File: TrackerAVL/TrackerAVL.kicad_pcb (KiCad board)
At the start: 2 copper layers, 120 x 80 mm, 174 parts, among them J801 Conn_02x07_Odd_Even, J802 Conn_01x15, J803 Conn_01x04, P201 uC_debug, Q201 DTC043ZEBTL, Q202 DTC043ZEBTL, Q203 DTC043ZEBTL, Q701 2N7002P, Q702 2N7002P, Q703 2N7002P, Q704 DTC043ZEBTL, U201 MAX3221, U202 LPC4337JBD144, U203 STS8C5H30L, U301 MPU-6050, U401 NAU8814, U501 STS8C5H30L, U502 LD1085D2T33R, U503 NCP114ASN180T1G, U601 MPCIE-Socket, U701 74LVC244APW, U801 74HC4053, X201 12MHz, X202 32.768K

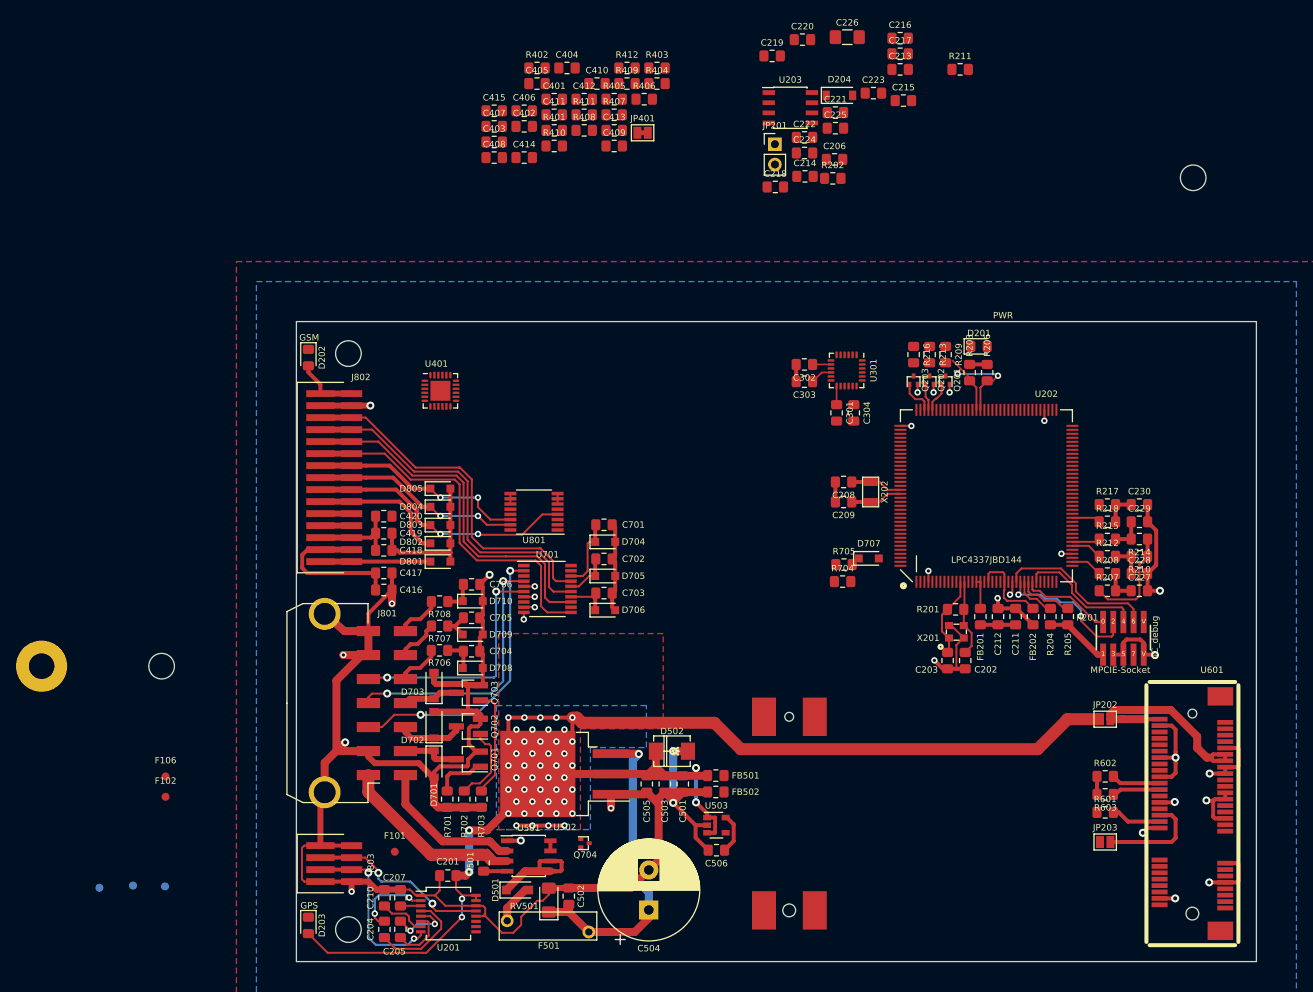
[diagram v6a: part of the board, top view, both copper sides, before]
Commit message: Cambios en pcb y modelos 3d
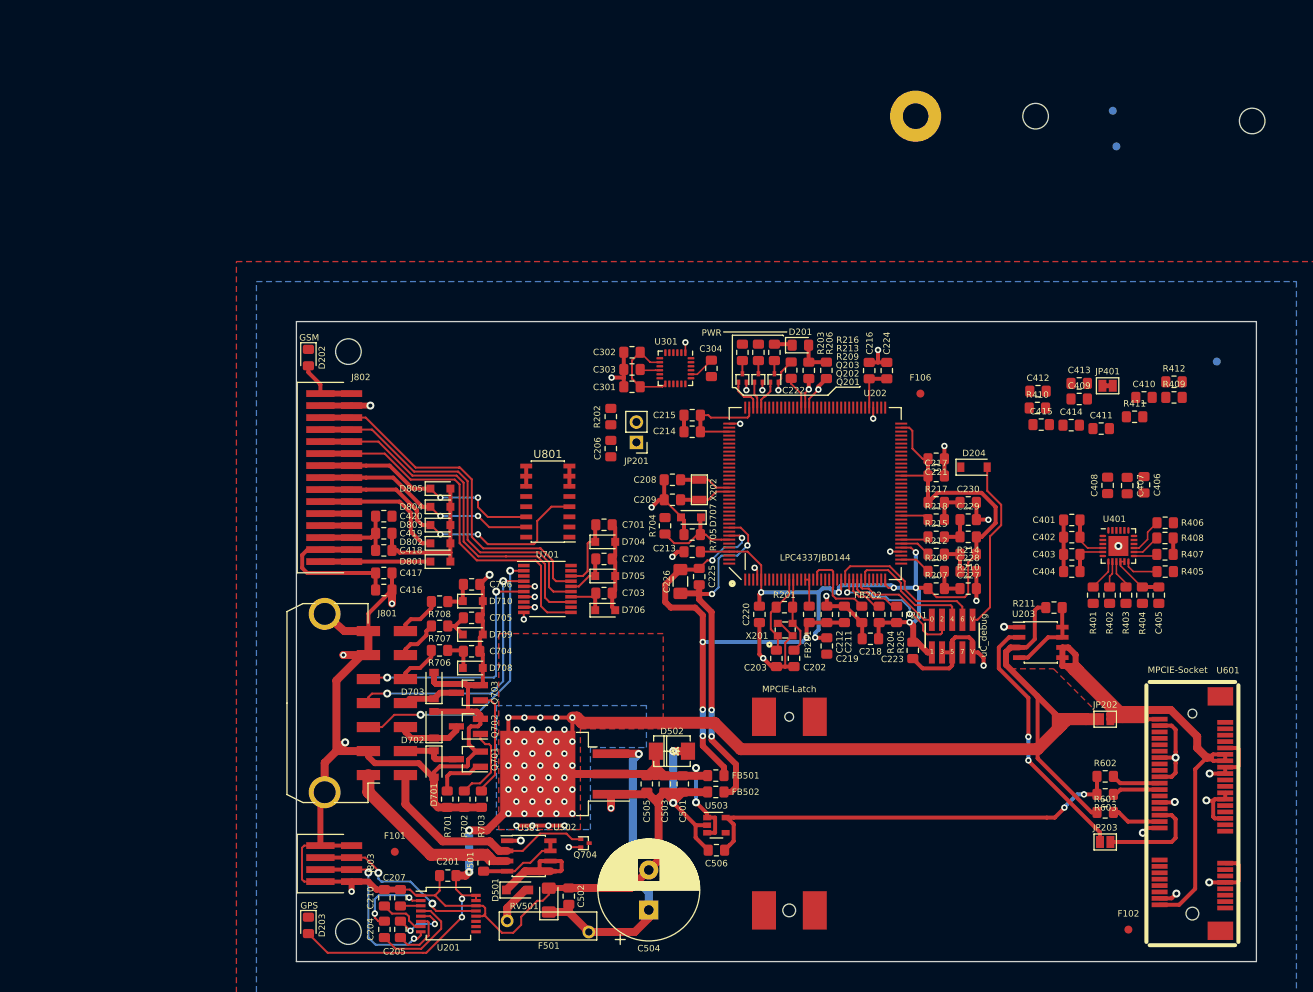
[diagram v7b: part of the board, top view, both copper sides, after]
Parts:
- U801: footprint Package_SO:TSSOP-16_4.4x5mm_P0.65mm -> Package_SO:SOIC-16_3.9x9.9mm_P1.27mm
- moved F103 157.3 mm to (212.5, 48.1)
- moved F104 156.1 mm to (212.1, 43.6)
- moved F105 146.9 mm to (225.1, 75.0)
- moved H102 129.1 mm to (202.4, 44.3)
- moved TP101 129.1 mm to (187.4, 44.3)
- moved F102 121.5 mm to (214.0, 146.0)
- moved F106 105.8 mm to (188.0, 79.0)
- moved C405 100.7 mm to (217.8, 104.2), turned to 270 degrees
- moved R402 97.3 mm to (211.7, 104.2), turned to 270 degrees
- moved C407 91.0 mm to (213.8, 90.5), turned to 270 degrees
- moved R405 90.7 mm to (218.6, 101.2)
- moved C406 90.5 mm to (215.9, 90.4), turned to 270 degrees
- moved C404 89.1 mm to (206.9, 101.2), turned to 180 degrees
- moved R401 89.0 mm to (209.6, 104.2), turned to 270 degrees
- moved C403 88.7 mm to (206.9, 99.1), turned to 180 degrees
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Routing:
- net +3V3: track 215.5 -> 387.0 mm, vias 52 -> 58
- net /CPU/PWR_MDM: track 27.7 -> 87.0 mm
- net +3.3VADC: track 4.40 -> 62.5 mm, vias 0 -> 6
- net +1V8: track 7.30 -> 62.8 mm, vias 0 -> 2
- net GND: track 366.3 -> 414.2 mm, vias 29 -> 38
- net GNDA: track 0.00 -> 46.1 mm, vias 0 -> 4
- net /CPU/GPIO7: track 0.00 -> 32.6 mm, vias 0 -> 2
- net /CPU/RESET_DBG: track 0.00 -> 21.6 mm
- net /CPU/VBAT: track 0.00 -> 11.4 mm
- net /IGN: track 18.8 -> 29.2 mm
- net Net-(R211-Pad1): track 0.00 -> 10.2 mm
- net Net-(C405-Pad1): track 0.00 -> 6.91 mm
- net Net-(R501-Pad1): track 4.22 -> 10.7 mm
- net /I2C_SCL: track 10.7 -> 4.52 mm, vias 2 -> 1
- net Net-(R406-Pad1): track 0.00 -> 4.71 mm
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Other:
- net class Default: via_dia 1 -> 0.8; via_drill 0.5 -> 0.4
- board text added: "MPCIE-Latch"
- board text added: "Net +3V3 Exclusiva PWR Módulo UC20"
- board text removed: "Eje central"

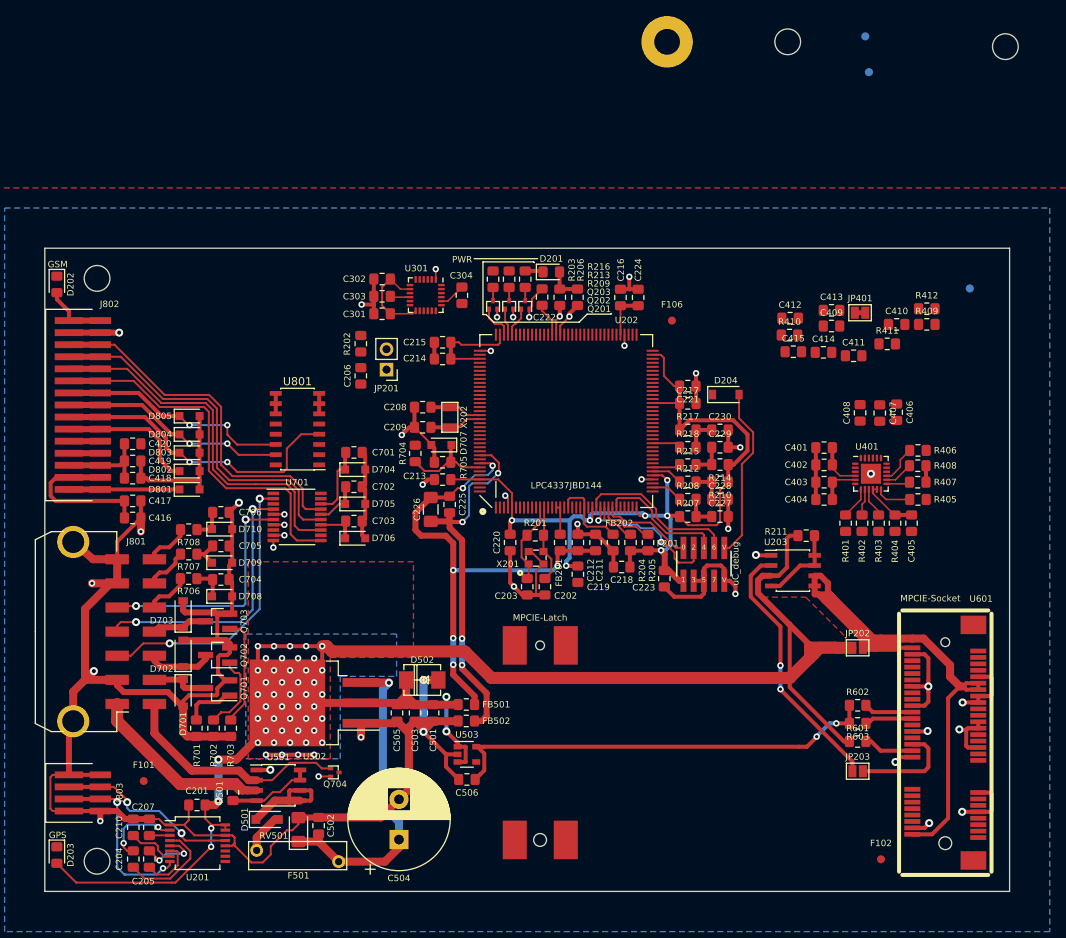
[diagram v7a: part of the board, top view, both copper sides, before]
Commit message: Cambios en pcb y modelos 3d
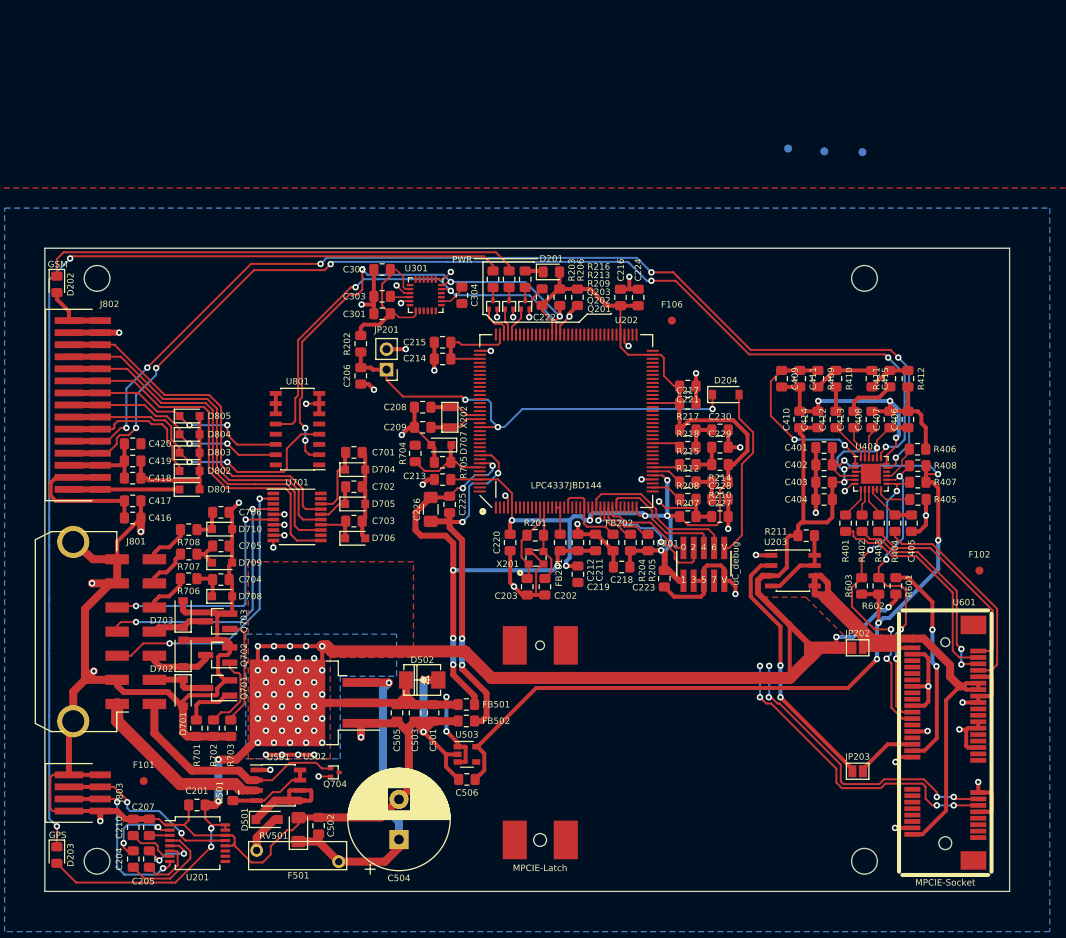
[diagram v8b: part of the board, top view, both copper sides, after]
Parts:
- removed TP101: TestPoint, MountingHole:MountingHole_3.2mm_M3_Pad
- JP401: footprint Jumper:SolderJumper-2_P1.3mm_Bridged_Pad1.0x1.5mm -> NetTie:NetTie-2_SMD_Pad0.5mm
- moved H103 102.8 mm to (211.9, 146.2)
- moved F102 37.9 mm to (226.2, 110.1)
- moved H102 30.9 mm to (211.9, 73.8)
- moved F105 21.6 mm to (211.7, 58.0)
- moved R601 19.9 mm to (215.8, 112.0), turned to 90 degrees
- moved R603 17.1 mm to (211.6, 112.0), turned to 90 degrees
- moved F104 16.9 mm to (202.4, 57.6)
- moved C410 16.9 mm to (203.9, 91.3), turned to 90 degrees
- moved JP401 15.3 mm to (219.0, 91.2), turned to 90 degrees
- moved R409 15.1 mm to (206.2, 86.2), turned to 270 degrees
- moved R602 15.1 mm to (213.7, 112.0), turned to 90 degrees
- moved C413 13.9 mm to (210.6, 91.3), turned to 90 degrees
- moved C412 13.8 mm to (208.4, 91.3), turned to 90 degrees
- moved F103 11.3 mm to (206.9, 58.0)
- moved C415 10.3 mm to (212.9, 86.2), turned to 270 degrees
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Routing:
- net /SPK+: track 3.90 -> 136.4 mm, vias 0 -> 6
- net /SPK-: track 3.90 -> 135.4 mm, vias 0 -> 6
- net Net-(D203-Pad1): track 0.00 -> 128.5 mm, vias 0 -> 2
- net +3V3: track 387.0 -> 450.8 mm, vias 58 -> 63
- net Net-(D202-Pad1): track 0.00 -> 60.1 mm
- net /I2C_SDA: track 3.81 -> 60.7 mm, vias 1 -> 5
- net /CPU/nRESET: track 0.00 -> 55.8 mm, vias 0 -> 3
- net /I2C_SCL: track 4.52 -> 58.1 mm, vias 1 -> 3
- net +1V8: track 62.8 -> 115.1 mm, vias 2 -> 5
- net GNDS: track 0.00 -> 41.8 mm, vias 1 -> 3
- net /CPU/U3_TX: track 0.00 -> 39.0 mm, vias 0 -> 4
- net /CPU/U3_RX: track 0.00 -> 37.3 mm, vias 0 -> 4
- net /UC20_PCIe/I2C_SCL: track 8.96 -> 40.8 mm, vias 0 -> 4
- net /UC20_PCIe/I2C_SDA: track 9.70 -> 38.9 mm, vias 0 -> 4
- net /Audio/ADCOUT: track 0.00 -> 27.6 mm
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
